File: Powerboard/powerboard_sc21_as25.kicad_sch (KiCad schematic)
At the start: 44 parts

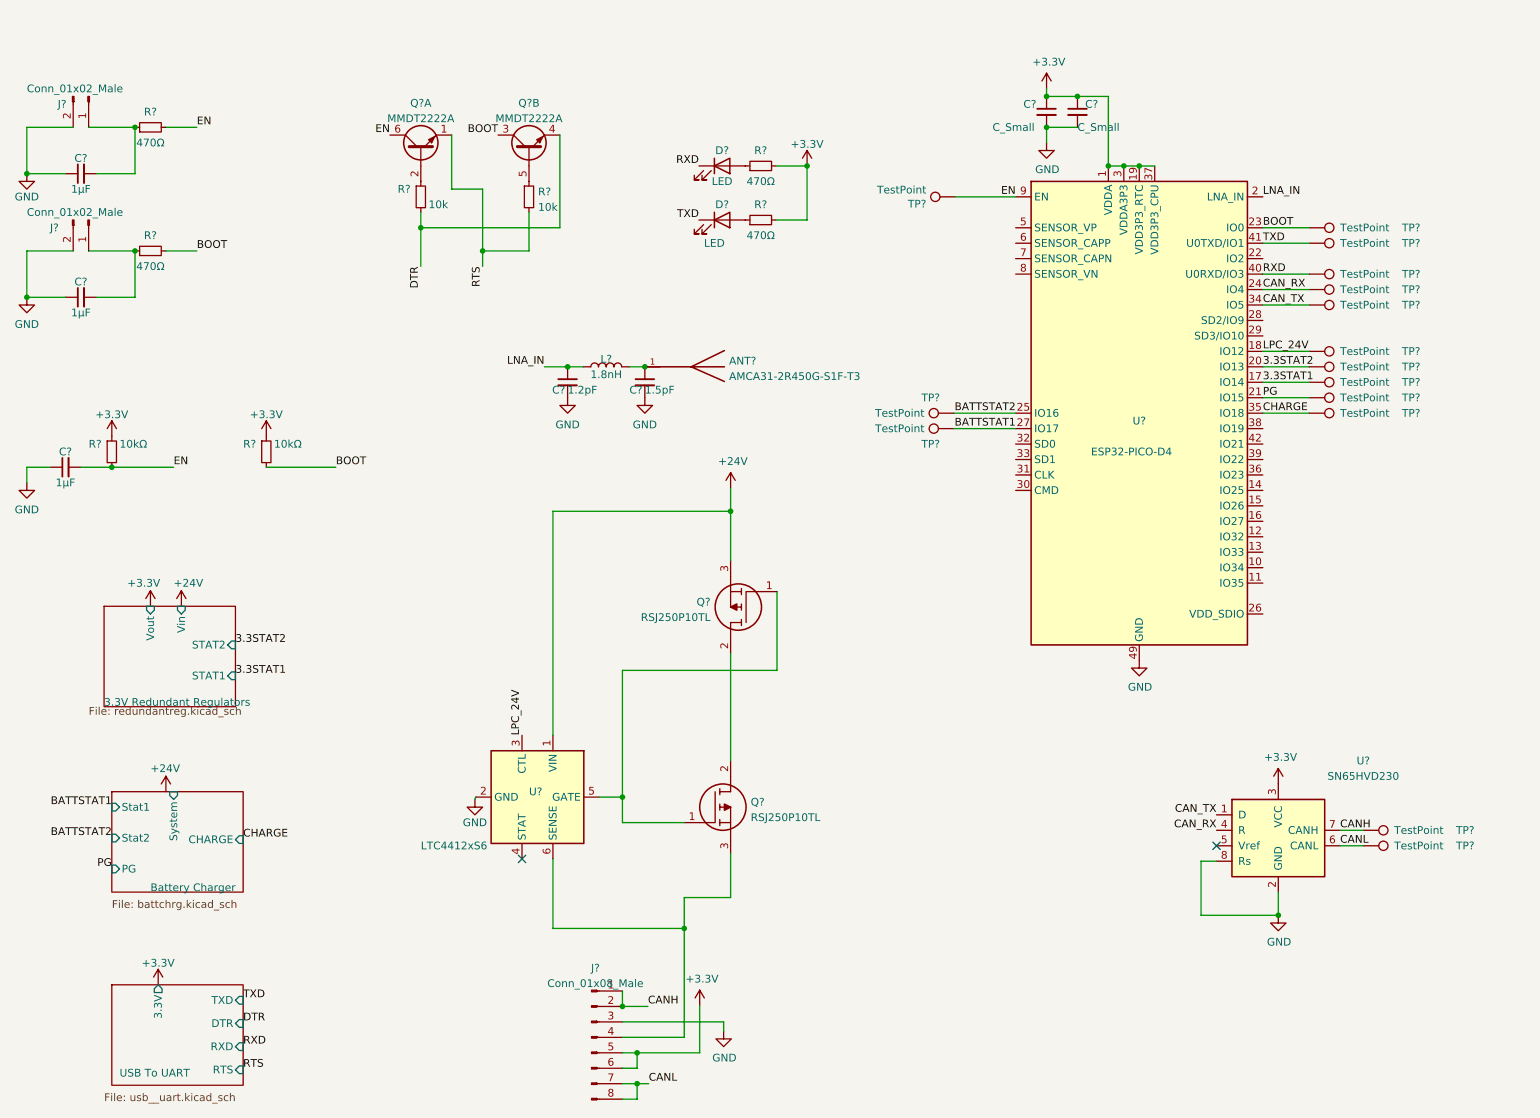
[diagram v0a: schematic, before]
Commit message: removed charger reverse polarity protection
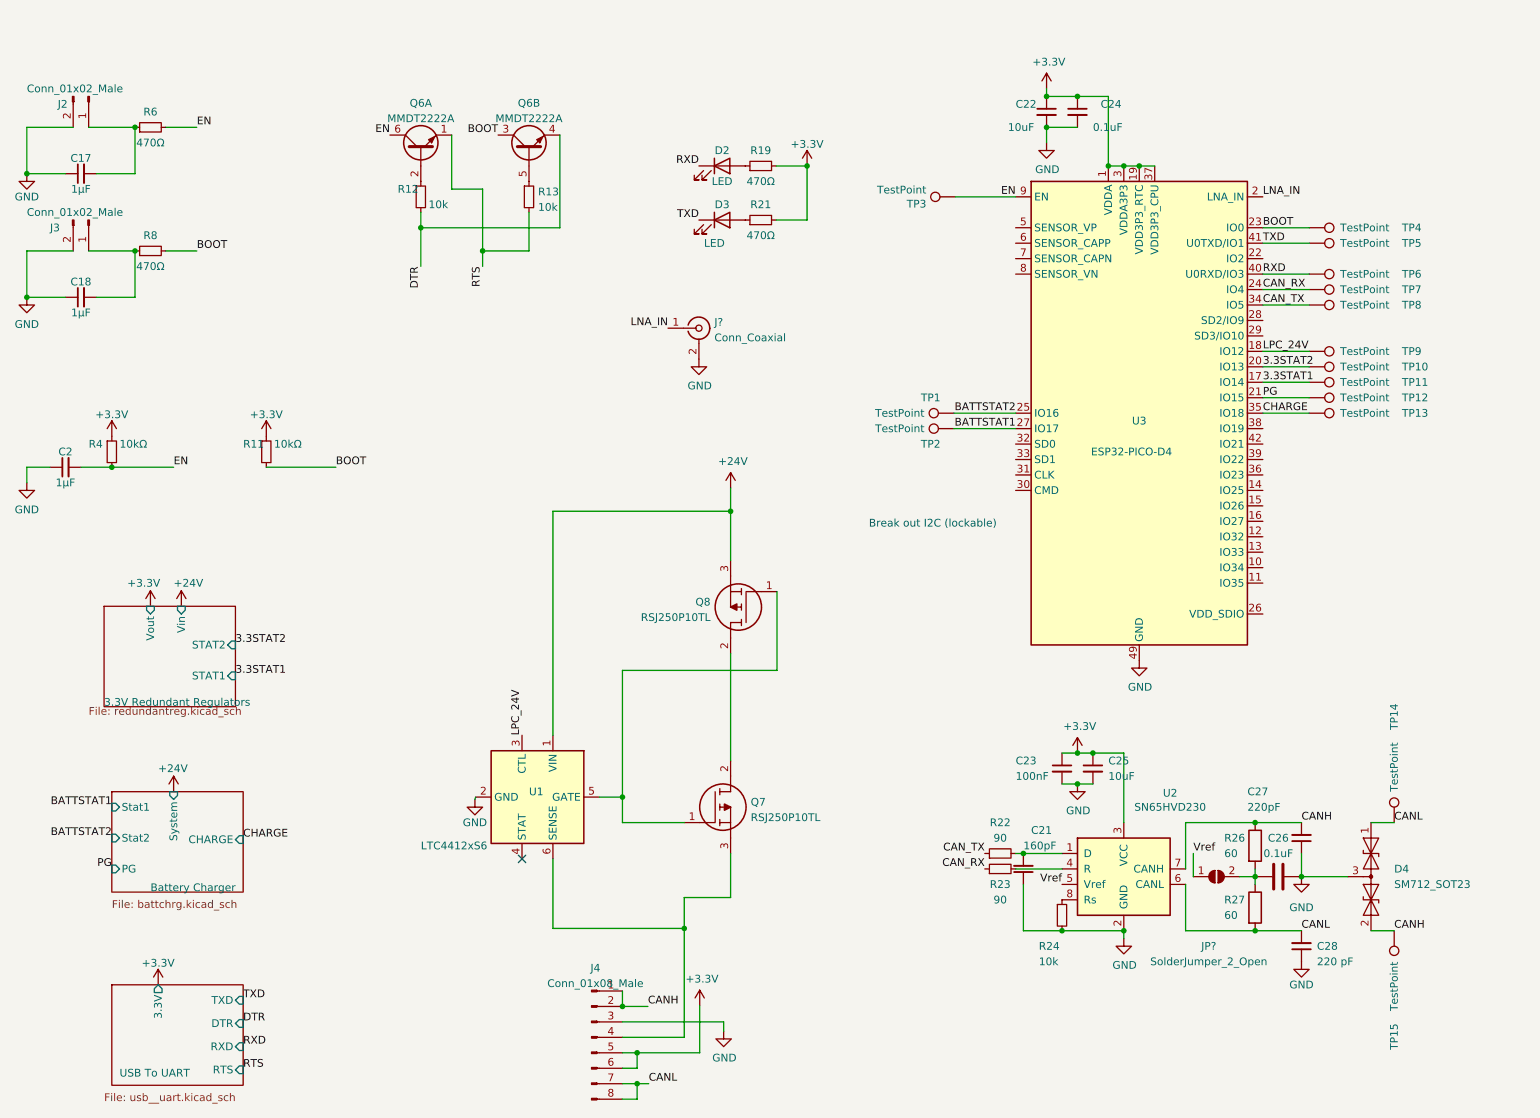
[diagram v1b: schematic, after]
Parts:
- removed ANT?: AMCA31-2R450G-S1F-T3, ANT_AMCA31-2R450G-S1F-T3, symbol iclr:AMCA31-2R450G-S1F-T3
- removed C?: 1.2pF, symbol Device:C_Small
- removed C?: 1.5pF, symbol Device:C_Small
- removed L?: 1.8nH, symbol Device:L
- removed TP? (x2): TestPoint, symbol Connector:TestPoint
- removed U?: SN65HVD230, Package_SO:SOIC-8_3.9x4.9mm_P1.27mm, symbol Interface_CAN_LIN:SN65HVD230
- added C21: 160pF, Capacitor_SMD:C_0603_1608Metric, symbol Device:C_Small
- added C23: 100nF, Capacitor_SMD:C_0603_1608Metric, symbol Device:C_Small
- added C25: 10uF, Capacitor_SMD:C_0603_1608Metric, symbol Device:C_Small
- added C26: 0.1uF, Capacitor_SMD:C_0603_1608Metric, symbol Device:C
- added C27: 220pF, Capacitor_SMD:C_0603_1608Metric, symbol Device:C_Small
- added C28: 220 pF, Capacitor_SMD:C_0603_1608Metric, symbol Device:C_Small
- added D4: SM712_SOT23, Package_TO_SOT_SMD:SOT-23, symbol Diode:SM712_SOT23
- added J?: Conn_Coaxial, Connector_Coaxial:U.FL_Molex_MCRF_73412-0110_Vertical, symbol Connector:Conn_Coaxial
- added JP?: SolderJumper_2_Open, symbol Jumper:SolderJumper_2_Open
- added R22, R23: 90, Resistor_SMD:R_0603_1608Metric, symbol Device:R_Small
- added R24: 10k, Resistor_SMD:R_0603_1608Metric, symbol Device:R_Small
- added R26, R27: 60, Resistor_SMD:R_0805_2012Metric, symbol Device:R
- added TP14, TP15: TestPoint, symbol Connector:TestPoint
- added U2: SN65HVD230, Package_SO:SOIC-8_3.9x4.9mm_P1.27mm, symbol Interface_CAN_LIN:SN65HVD230
- C22: renamed from C?; value C_Small -> 10uF
- C24: renamed from C?; value C_Small -> 0.1uF
- gave numbers to parts that had none: 34
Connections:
- net +3V3: now also C23.1, C25.1, U2.3 (VCC)
- net CANH: now also C27.2, D4.2 (A2), R26.1, TP15.1, U2.7 (CANH)
- net CANL: now also C28.2, D4.1 (A1), R27.2, TP14.1, U2.6 (CANL)
- net CAN_RX: now also R23.1
- net CAN_TX: now also R22.1
- net GND: now also C21.1, C23.2, C25.2, C26.2, C27.1, C28.1, D4.3 (common), J?.2 (Ext), R24.2, U2.2 (GND)
- net LNA_IN: now also J?.1 (In)
- new net: C21.2, R22.2, U2.1 (D)
- new net: R23.2, U2.4 (R)
- new net: R24.1, U2.8 (Rs)
- new net: C26.1, JP?.2 (B), R26.2, R27.1
- new net Vref: JP?.1 (A), U2.5 (Vref)
- no-connect marks 2 -> 1
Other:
- note added: "Break out I2C (lockable)"
